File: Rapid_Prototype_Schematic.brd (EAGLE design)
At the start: 142 x 95 mm, 177 parts, among them IC2 SI4459ADY-T1-GE3, IC8 SI4485DY-T1-GE3, J1 XT60-M, J10 XT60-M, J2 XT60-M, J3 Vertical Qwiic Connector, J4 UJ2-MIBH-2-SMT-TR-67, J5 XT60-M, J6 XT60-M, J7 XT60-M, J8 XT60-M, J9 XT60-M, Q1 LTV-8141S, Q10 SI4435DDY, Q11 DMN65D8LFB-7, Q12 SI4435DDY, Q13 DMN65D8LFB-7, Q14 SI4435DDY, Q15 DMN65D8LFB-7, Q16 2N7002PW, Q2 2N7002PW, Q3 DMN65D8LFB-7, Q4 SI4435DDY, Q5 DMN65D8LFB-7, Q6 SI4435DDY, Q7 DMN65D8LFB-7, Q8 SI4435DDY, Q9 DMN65D8LFB-7, U1 LM35DM, U2 LM2904ITPX/NOPB, U3 LM2904ITPX/NOPB, U4 LM2904ITPX/NOPB, U5 LM2904ITPX/NOPB, U6 LM2904ITPX/NOPB, U7 TLV1117LV33DCYR, U8 LT1374IS8-5PBF

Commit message: Resistor changes
Changed Resistor Power outputs to 0.001
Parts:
- R26, R67: value 0.8Ω 1% -> 0.001Ω 1%
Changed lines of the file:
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@@
 <attribute name="VALUE" x="102.295959375" y="87.254078125" size="1.27" layer="27"/>
 </element>
-<element name="R26" library="rcl" library_urn="urn:adsk.eagle:library:334" package="R2512" package3d_urn="urn:adsk.eagle:package:23545/2" value="0.8Ω 1%" x="108.666278125" y="86.426959375" smashed="yes" rot="R270">
+<element name="R26" library="rcl" library_urn="urn:adsk.eagle:library:334" package="R2512" package3d_urn="urn:adsk.eagle:package:23545/2" value="0.001Ω 1%" x="108.666278125" y="86.426959375" smashed="yes" rot="R270">
 <attribute name="NAME" x="109.809278125" y="87.823959375" size="0.8128" layer="25" rot="R270"/>
 <attribute name="POPULARITY" value="0" x="108.666278125" y="86.426959375" size="1.778" layer="27" rot="R270" display="off"/>
@@
 <attribute name="VALUE" x="68.839078125" y="37.317678125" size="0.6096" layer="27" font="vector" ratio="20" rot="R180"/>
 </element>
-<element name="R67" library="rcl" library_urn="urn:adsk.eagle:library:334" package="R2512" package3d_urn="urn:adsk.eagle:package:23545/2" value="0.8Ω 1%" x="108.671359375" y="78.232" smashed="yes" rot="R90">
+<element name="R67" library="rcl" library_urn="urn:adsk.eagle:library:334" package="R2512" package3d_urn="urn:adsk.eagle:package:23545/2" value="0.001Ω 1%" x="108.671359375" y="78.232" smashed="yes" rot="R90">
 <attribute name="NAME" x="106.766359375" y="75.692" size="1.27" layer="25" rot="R90"/>
 <attribute name="POPULARITY" value="0" x="108.671359375" y="78.232" size="1.778" layer="27" rot="R90" display="off"/>

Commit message: Capacitor typo
Changed the C34 package to uf rather than mf
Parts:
- C34: value 0.1 mf -> 0.1 uf
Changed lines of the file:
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@@
 <attribute name="VALUE" x="61.976" y="88.519" size="1.27" layer="27" rot="R270"/>
 </element>
-<element name="C34" library="adafruit" library_urn="urn:adsk.eagle:library:420" package="C0603" package3d_urn="urn:adsk.eagle:package:6240338/1" value="0.1 mf" x="54.483" y="22.479" smashed="yes" rot="R90">
+<element name="C34" library="adafruit" library_urn="urn:adsk.eagle:library:420" package="C0603" package3d_urn="urn:adsk.eagle:package:6240338/1" value="0.1 uf" x="54.483" y="22.479" smashed="yes" rot="R90">
 <attribute name="NAME" x="53.721" y="21.59" size="0.8128" layer="25" rot="R90"/>
 <attribute name="VALUE" x="56.515" y="21.59" size="1.27" layer="27" rot="R90"/>

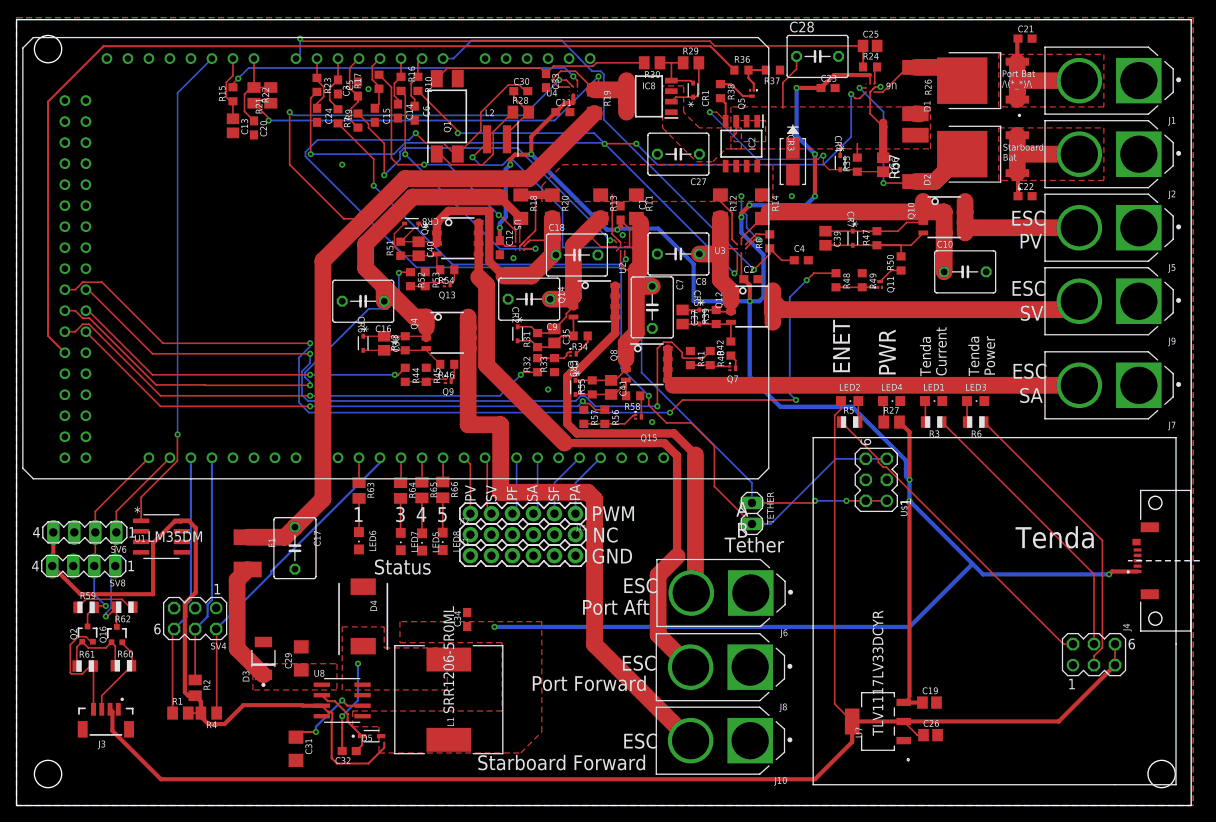
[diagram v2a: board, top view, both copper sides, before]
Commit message: Compasitors
Changed the capacitors to the correct 3.5mm pitch.
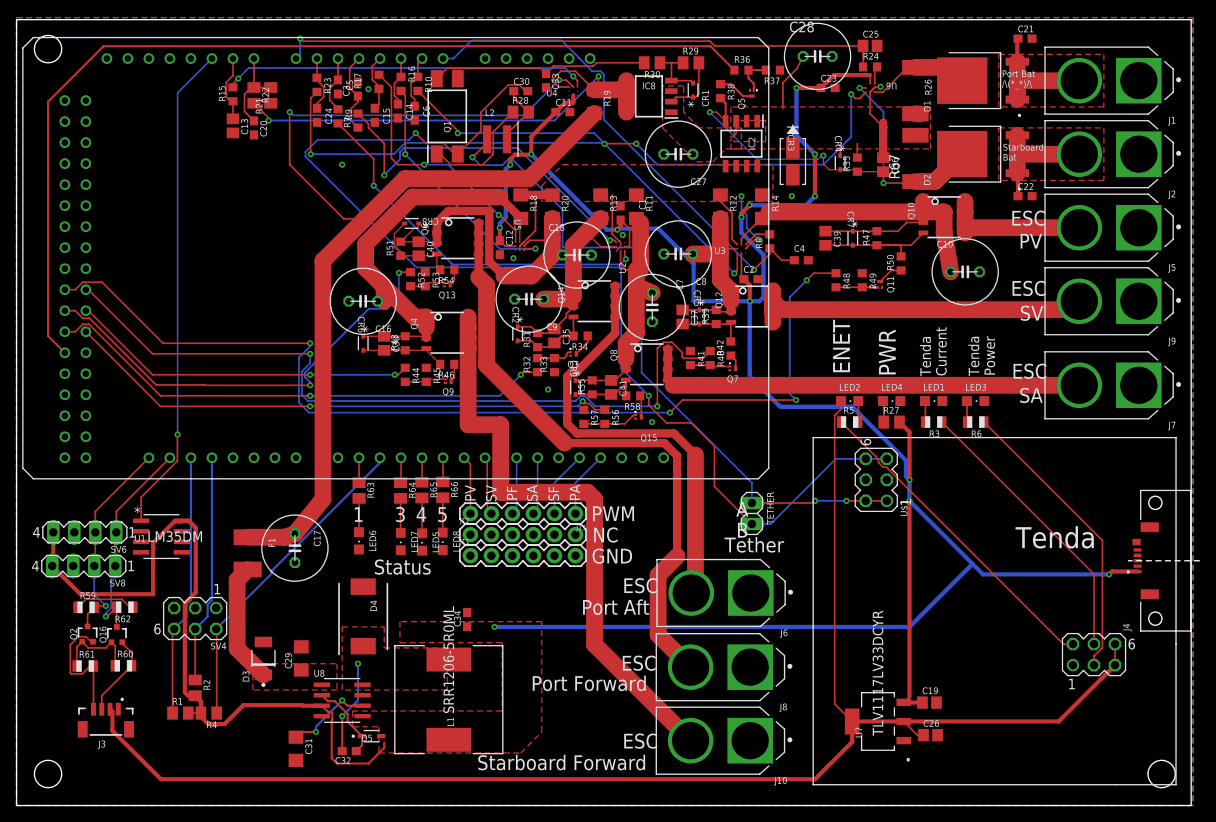
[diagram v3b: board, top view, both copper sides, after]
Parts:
- C10, C16, C17, C18, C27, C28, C7, C8, C9: device adafruit:C050-050X075 -> Rapid_Prototype_Schematic:3.5MMCAP
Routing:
- net ESC_PF_POWER: track 41.4 -> 42.2 mm
- net ESC_SV_POWER: track 22.6 -> 23.4 mm
- net ESC_PA_POWER: track 28.2 -> 29.0 mm
- net ESC_SF_POWER: track 49.9 -> 50.7 mm
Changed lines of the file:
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@@
 <attribute name="VALUE" x="75.057" y="70.739" size="1.27" layer="27" rot="R90"/>
 </element>
-<element name="C10" library="adafruit" library_urn="urn:adsk.eagle:library:420" package="C050-050X075" package3d_urn="urn:adsk.eagle:package:6240360/1" value="220µF" x="114.681" y="64.516" smashed="yes">
+<element name="C10" library="Rapid_Prototype_Schematic" package="3.5MMCAP" value="220µF" x="114.681" y="64.516" smashed="yes">
 <attribute name="NAME" x="111.252" y="67.437" size="0.8128" layer="25" ratio="10"/>
 <attribute name="VALUE" x="111.506" y="62.357" size="1.27" layer="27" ratio="10"/>
@@
 <attribute name="VALUE" x="41.021" y="84.328" size="1.27" layer="27" rot="R270"/>
 </element>
-<element name="C16" library="adafruit" library_urn="urn:adsk.eagle:library:420" package="C050-050X075" package3d_urn="urn:adsk.eagle:package:6240360/1" value="220µF" x="41.91" y="60.96" smashed="yes" rot="R180">
+<element name="C16" library="Rapid_Prototype_Schematic" package="3.5MMCAP" value="220µF" x="41.91" y="60.96" smashed="yes" rot="R180">
 <attribute name="NAME" x="45.339" y="58.039" size="0.8128" layer="25" ratio="10" rot="R180"/>
 <attribute name="VALUE" x="45.085" y="63.119" size="1.27" layer="27" ratio="10" rot="R180"/>
 </element>
-<element name="C17" library="adafruit" library_urn="urn:adsk.eagle:library:420" package="C050-050X075" package3d_urn="urn:adsk.eagle:package:6240360/1" value="220uF" x="33.655" y="31.115" smashed="yes" rot="R270">
+<element name="C17" library="Rapid_Prototype_Schematic" package="3.5MMCAP" value="220uF" x="33.655" y="31.115" smashed="yes" rot="R270">
 <attribute name="NAME" x="35.941" y="33.274" size="0.8128" layer="25" ratio="10" rot="R270"/>
 <attribute name="VALUE" x="31.496" y="34.29" size="1.27" layer="27" ratio="10" rot="R270"/>
 </element>
-<element name="C18" library="adafruit" library_urn="urn:adsk.eagle:library:420" package="C050-050X075" package3d_urn="urn:adsk.eagle:package:6240360/1" value="220µF" x="67.7443375" y="66.548" smashed="yes">
+<element name="C18" library="Rapid_Prototype_Schematic" package="3.5MMCAP" value="220µF" x="67.7443375" y="66.548" smashed="yes">
 <attribute name="NAME" x="64.3153375" y="69.469" size="0.8128" layer="25" ratio="10"/>
 <attribute name="VALUE" x="64.5693375" y="64.389" size="1.27" layer="27" ratio="10"/>
@@
 <attribute name="VALUE" x="109.601" y="6.223" size="1.27" layer="27"/>
 </element>
-<element name="C27" library="adafruit" library_urn="urn:adsk.eagle:library:420" package="C050-050X075" package3d_urn="urn:adsk.eagle:package:6240360/1" value="220µF" x="80.01" y="78.74" smashed="yes" rot="R180">
+<element name="C27" library="Rapid_Prototype_Schematic" package="3.5MMCAP" value="220µF" x="80.01" y="78.74" smashed="yes" rot="R180">
 <attribute name="NAME" x="83.439" y="75.819" size="0.8128" layer="25" ratio="10" rot="R180"/>
 <attribute name="VALUE" x="83.185" y="80.899" size="1.27" layer="27" ratio="10" rot="R180"/>
 </element>
-<element name="C28" library="adafruit" library_urn="urn:adsk.eagle:library:420" package="C050-050X075" package3d_urn="urn:adsk.eagle:package:6240360/1" value="220µF" x="96.834959375" y="90.556078125" smashed="yes">
+<element name="C28" library="Rapid_Prototype_Schematic" package="3.5MMCAP" value="220µF" x="96.834959375" y="90.556078125" smashed="yes">
 <attribute name="NAME" x="93.405959375" y="93.477078125" size="1.27" layer="25" ratio="10"/>
 <attribute name="VALUE" x="93.659959375" y="88.397078125" size="1.27" layer="27" ratio="10"/>
@@
 <attribute name="VALUE" x="45.847" y="84.582" size="1.27" layer="27" rot="R270"/>
 </element>
-<element name="C7" library="adafruit" library_urn="urn:adsk.eagle:library:420" package="C050-050X075" package3d_urn="urn:adsk.eagle:package:6240360/1" value="220µF" x="76.852778125" y="60.220859375" smashed="yes" rot="R270">
+<element name="C7" library="Rapid_Prototype_Schematic" package="3.5MMCAP" value="220µF" x="76.852778125" y="60.220859375" smashed="yes" rot="R270">
 <attribute name="NAME" x="79.773778125" y="63.649859375" size="0.8128" layer="25" ratio="10" rot="R270"/>
 <attribute name="VALUE" x="74.693778125" y="63.395859375" size="1.27" layer="27" ratio="10" rot="R270"/>
 </element>
-<element name="C8" library="adafruit" library_urn="urn:adsk.eagle:library:420" package="C050-050X075" package3d_urn="urn:adsk.eagle:package:6240360/1" value="220µF" x="80.01" y="66.675" smashed="yes" rot="R180">
+<element name="C8" library="Rapid_Prototype_Schematic" package="3.5MMCAP" value="220µF" x="80.01" y="66.675" smashed="yes" rot="R180">
 <attribute name="NAME" x="83.439" y="63.754" size="0.8128" layer="25" ratio="10" rot="R180"/>
 <attribute name="VALUE" x="83.185" y="68.834" size="1.27" layer="27" ratio="10" rot="R180"/>
 </element>
-<element name="C9" library="adafruit" library_urn="urn:adsk.eagle:library:420" package="C050-050X075" package3d_urn="urn:adsk.eagle:package:6240360/1" value="220µF" x="61.970921875" y="61.214" smashed="yes" rot="R180">
+<element name="C9" library="Rapid_Prototype_Schematic" package="3.5MMCAP" value="220µF" x="61.970921875" y="61.214" smashed="yes" rot="R180">
 <attribute name="NAME" x="65.399921875" y="58.293" size="0.8128" layer="25" ratio="10" rot="R180"/>
 <attribute name="VALUE" x="65.145921875" y="63.373" size="1.27" layer="27" ratio="10" rot="R180"/>
@@
 <wire x1="104.013" y1="69.43" x2="106.553" y2="69.43" width="0.2032" layer="1"/>
 <wire x1="109.6135" y1="73.025" x2="109.6135" y2="71.755" width="2.032" layer="1"/>
-<wire x1="112.141" y1="69.2275" x2="112.141" y2="64.516" width="2.032" layer="1"/>
+<wire x1="112.141" y1="69.2275" x2="112.931" y2="64.516" width="2.032" layer="1"/>
 <wire x1="87.63" y1="68.58" x2="90.018" y2="70.968" width="0.2032" layer="1"/>
 <wire x1="90.018" y1="70.968" x2="90.17" y2="70.968" width="0.2032" layer="1"/>
@@
 <wire x1="82.55" y1="59.9074" x2="80.5204" y2="59.9074" width="0.2032" layer="1"/>
 <wire x1="80.5204" y1="59.9074" x2="80.518" y2="59.905" width="0.2032" layer="1"/>
-<wire x1="82.55" y1="66.675" x2="85.09" y2="66.675" width="2.032" layer="1"/>
+<wire x1="81.76" y1="66.675" x2="85.09" y2="66.675" width="2.032" layer="1"/>
 <wire x1="85.725" y1="67.31" x2="85.09" y2="66.675" width="0.2032" layer="1"/>
 <wire x1="87.13" y1="67.31" x2="85.725" y2="67.31" width="0.2032" layer="1"/>
@@
 <wire x1="64.77" y1="68.58" x2="64.77" y2="70.968" width="2.032" layer="1"/>
 <wire x1="64.77" y1="68.58" x2="64.516" y2="68.326" width="0.1524" layer="1"/>
-<wire x1="64.77" y1="66.548" x2="65.2043375" y2="66.548" width="1.016" layer="1"/>
+<wire x1="64.77" y1="66.548" x2="65.9943375" y2="66.548" width="1.016" layer="1"/>
 <wire x1="64.77" y1="66.548" x2="62.23" y2="64.008" width="2.032" layer="1"/>
 <wire x1="46.4413625" y1="68.16" x2="48.1004625" y2="69.8191" width="0.1524" layer="1"/>
@@
 <wire x1="64.516" y1="57.111" x2="62.992" y2="57.111" width="0.2032" layer="1"/>
 <wire x1="67.3225" y1="61.595" x2="66.9415" y2="61.214" width="2.032" layer="1"/>
-<wire x1="66.9415" y1="61.214" x2="64.510921875" y2="61.214" width="2.032" layer="1"/>
+<wire x1="66.9415" y1="61.214" x2="63.720921875" y2="61.214" width="2.032" layer="1"/>
 <wire x1="65.024" y1="57.619" x2="65.024" y2="57.9374" width="0.2032" layer="1"/>
 <wire x1="67.3225" y1="62.865" x2="67.3225" y2="67.6785" width="2.032" layer="1"/>
@@
 <wire x1="75.438" y1="70.46" x2="74.93" y2="70.968" width="1.016" layer="1"/>
 <wire x1="75.438" y1="70.46" x2="75.438" y2="64.77" width="2.032" layer="1"/>
-<wire x1="74.93" y1="62.760859375" x2="76.852778125" y2="62.760859375" width="2.032" layer="1"/>
+<wire x1="74.93" y1="62.760859375" x2="76.852778125" y2="61.970859375" width="2.032" layer="1"/>
 <wire x1="73.025" y1="67.064" x2="73.025" y2="65.405" width="0.2032" layer="1"/>
 <wire x1="73.025" y1="65.405" x2="73.66" y2="64.77" width="0.2032" layer="1"/>
@@
 <wire x1="33.02" y1="77.47" x2="39.56733125" y2="70.92266875" width="0.2032" layer="1"/>
 <wire x1="39.56733125" y1="70.92266875" x2="42.10733125" y2="70.92266875" width="0.2032" layer="1"/>
-<wire x1="37.0396" y1="37.0396" x2="33.655" y2="33.655" width="2.032" layer="1"/>
+<wire x1="37.0396" y1="37.0396" x2="33.655" y2="32.865" width="2.032" layer="1"/>
 <wire x1="37.0396" y1="65.8549375" x2="37.0396" y2="37.0396" width="2.032" layer="1"/>
-<wire x1="33.655" y1="33.655" x2="32.43" y2="32.43" width="2.032" layer="1"/>
+<wire x1="33.655" y1="32.865" x2="32.43" y2="32.43" width="2.032" layer="1"/>
 <wire x1="32.43" y1="32.43" x2="27.94" y2="32.43" width="2.032" layer="1"/>
 </signal>
@@
 <wire x1="60.96" y1="70.968" x2="60.833" y2="70.968" width="0.1524" layer="1"/>
 <wire x1="60.833" y1="70.968" x2="60.833" y2="68.114803125" width="0.1524" layer="1"/>
-<wire x1="44.45" y1="60.96" x2="44.4409" y2="60.9691" width="1.016" layer="1"/>
+<wire x1="43.66" y1="60.96" x2="44.4409" y2="60.9691" width="1.016" layer="1"/>
 <wire x1="44.4409" y1="62.71855625" x2="44.4409" y2="60.9691" width="2.032" layer="1"/>
 </signal>
@@
 <vertex x="87.63" y="79.375"/>
 </polygon>
-<wire x1="94.294959375" y1="90.556078125" x2="94.294959375" y2="89.032078125" width="0.2032" layer="1"/>
+<wire x1="95.084959375" y1="90.556078125" x2="94.294959375" y2="89.032078125" width="0.2032" layer="1"/>
 <wire x1="94.294959375" y1="89.032078125" x2="92.646759375" y2="87.383878125" width="0.2032" layer="1"/>
 <wire x1="92.646759375" y1="87.383878125" x2="92.646759375" y2="84.3054375" width="0.2032" layer="1"/>

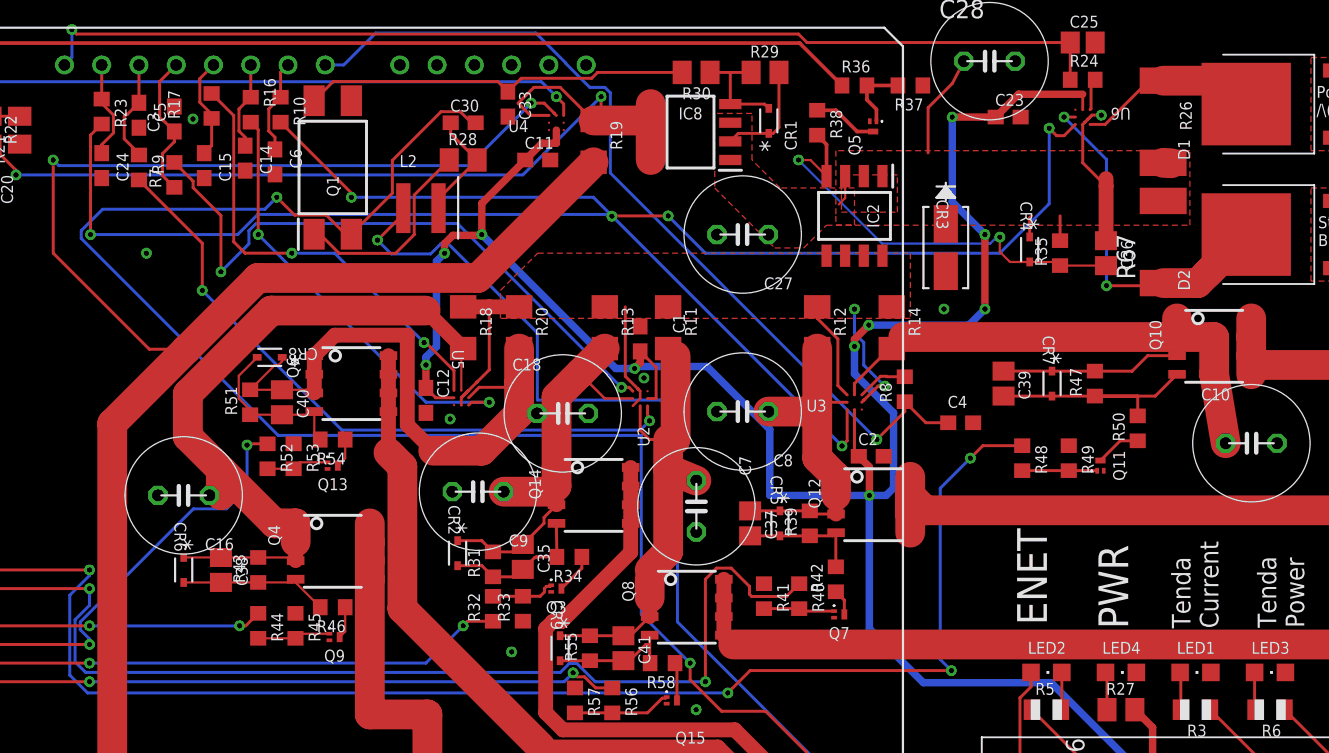
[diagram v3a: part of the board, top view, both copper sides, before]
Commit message: Capacitor Overlap Changes
Changed the capacitor positions in order to fit them flush to the board.
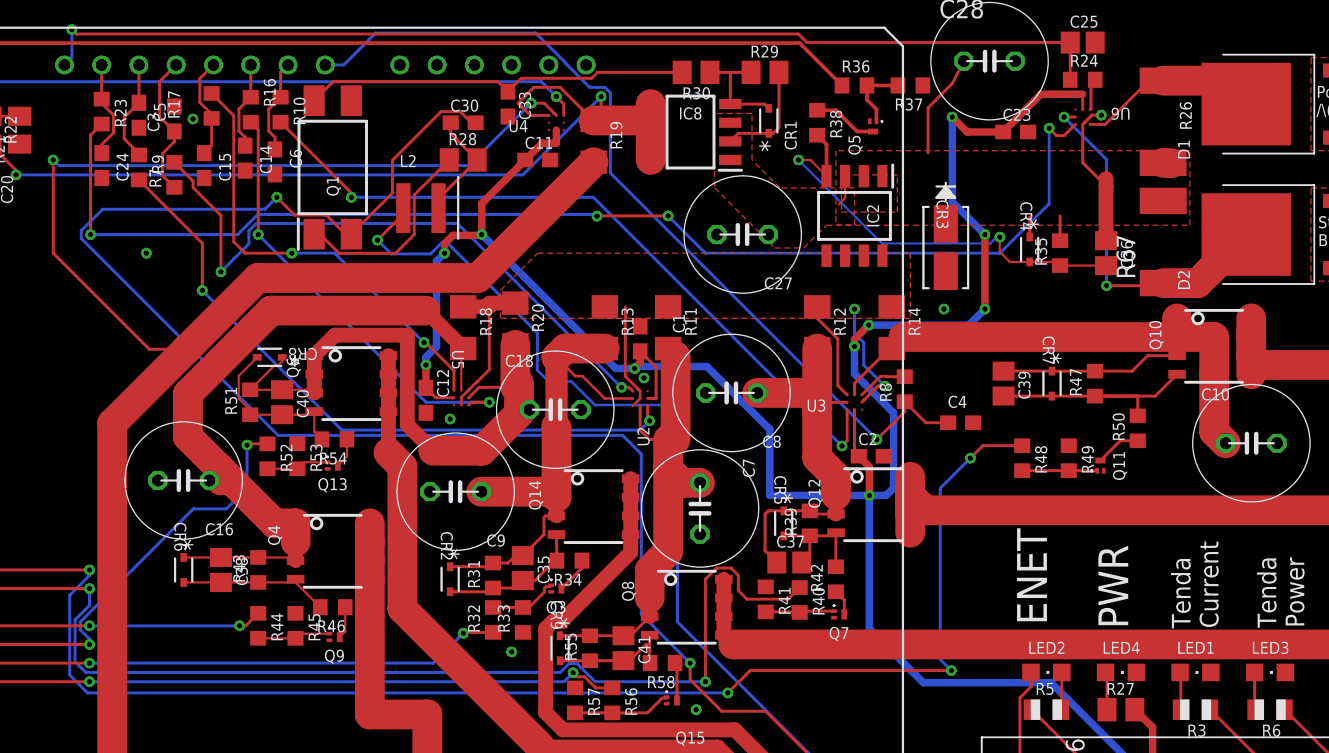
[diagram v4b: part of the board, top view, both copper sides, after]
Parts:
- moved C37 3.77 mm to (83.2, 56.4), turned to 0 degrees
- moved CR2 1.85 mm to (60.1, 55.2)
- moved C9 1.52 mm to (60.4, 61.2)
- moved C8 1.48 mm to (79.2, 67.9)
- moved C23 1.14 mm to (98.6, 85.7)
- moved C16 1.02 mm to (41.9, 62.0)
- moved C35 0.76 mm to (65.0, 56.0)
- moved Q14 0.76 mm to (69.8, 60.2)
- moved R31 0.76 mm to (63.0, 55.5)
- moved R32 0.76 mm to (63.0, 52.5)
- moved R33 0.76 mm to (65.0, 52.5)
- moved C18 0.57 mm to (67.2, 66.8)
- moved R20 0.36 mm to (64.5, 72.6)
- moved C7 0.29 mm to (77.1, 60.1)
- moved R40 0.27 mm to (83.9, 53.8)
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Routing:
- net ESC_PA_POWER: track 29.0 -> 36.1 mm
- net ESC_SV_POWER: track 23.4 -> 26.9 mm
- net TETHER_A: track 83.3 -> 82.1 mm
- net ESC_SF_POWER: track 50.7 -> 49.7 mm
- net 5V: track 372.8 -> 373.6 mm
- net ESCPA_POWER: track 53.4 -> 52.7 mm
- net TETHER_B: track 137.1 -> 136.4 mm
- net ESC_POWER: track 34.6 -> 33.9 mm
